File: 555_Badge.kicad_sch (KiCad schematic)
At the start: 13 parts

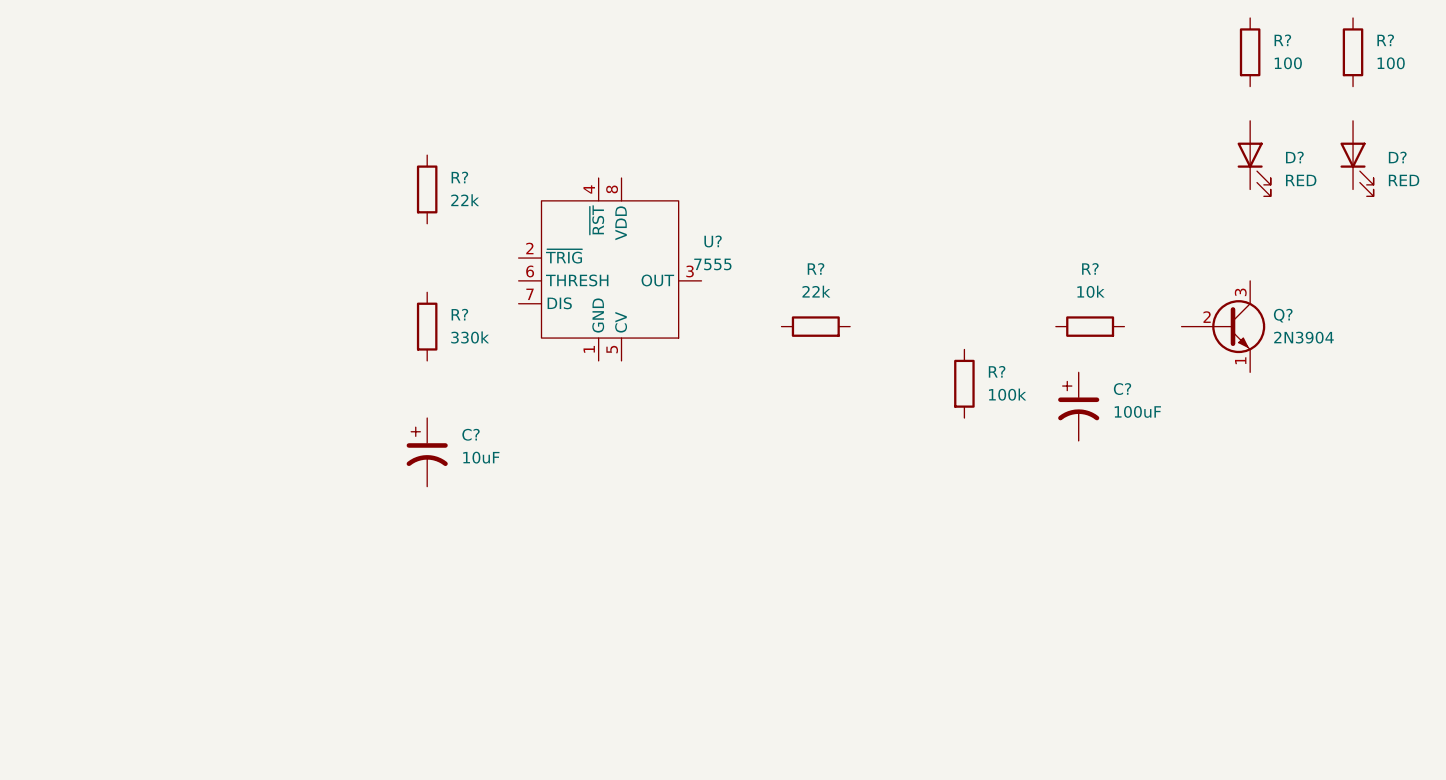
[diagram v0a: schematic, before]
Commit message: Small changes to the badge symbol and finished schematic
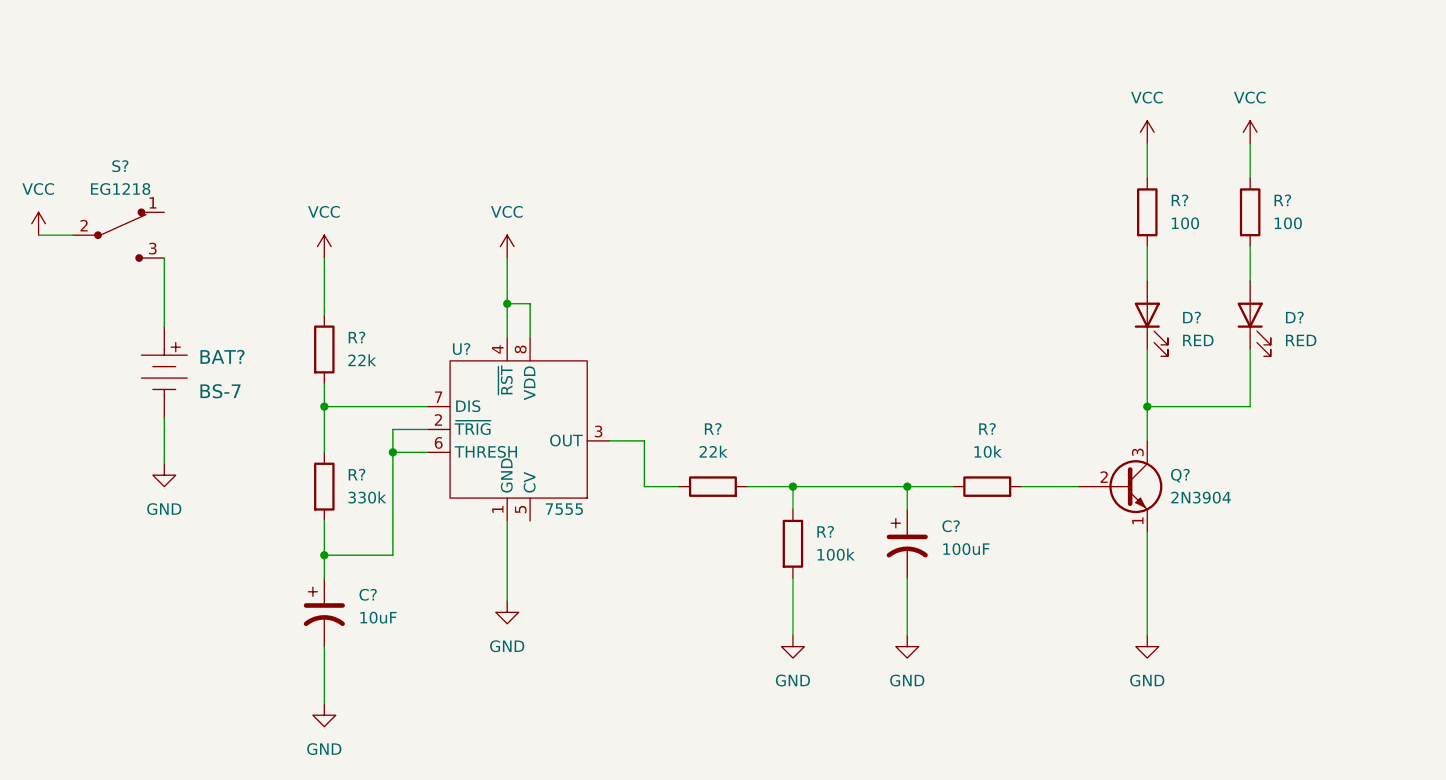
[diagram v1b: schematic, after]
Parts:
- added BAT?: BS-7, digikey-footprints:Battery_Holder_Coin_2032_BS-7, symbol dk_Battery-Holders-Clips-Contacts:BS-7
- added S?: EG1218, digikey-footprints:Switch_Slide_11.6x4mm_EG1218, symbol dk_Slide-Switches:EG1218
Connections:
- net at D?.1 (K): now also D?.1 (K), Q?.3 (C)
- net at D?.2 (A): now also R?.2 (x2)
- net at R?.1: now also C?.1, R?.1, R?.2
- net GND: now reaches R?.2
- net GND: now also C?.2, C?.2, Q?.1 (E), U?.1 (GND), BAT?.Neg
- net at R?.2: now also Q?.2 (B)
- net at U?.2 (~{TRIG}): now also C?.1, R?.2, U?.6 (THRESH)
- net at U?.3 (OUT): now also R?.1
- net VCC: now reaches U?.4 (~{RST})
- net VCC: now also R?.1, R?.1, R?.1, U?.8 (VDD), S?.2
- net at U?.7 (DIS): now also R?.1, R?.2
- new net: BAT?.Pos, S?.3
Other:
- moved on the sheet: C?, D?, Q?, R?, U?

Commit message: More changes to schematic. Numbered all of my resistors and capacitors
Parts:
- gave numbers to parts that had none: 15

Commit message: Lot of work on schematic and PCB to place components and begin constructing the PCB layout
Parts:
- C1: footprint (none) -> Capacitor_THT:CP_Radial_D5.0mm_P2.00mm
- C2: footprint (none) -> Capacitor_THT:CP_Radial_D6.3mm_P2.50mm
- D1, D2: footprint (none) -> LED_THT:LED_D3.0mm
- Q1: footprint Package_TO_SOT_THT:TO-92_Inline -> digikey-footprints:TO-92-3
- R1, R2, R3, R4, R5, R6, R7: footprint (none) -> Resistor_THT:R_Axial_DIN0207_L6.3mm_D2.5mm_P7.62mm_Horizontal
- U1: footprint (none) -> 555_Badge:ICM7555-PDIP
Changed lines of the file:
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@@
       (effects (font (size 1.27 1.27)) (justify right))
     )
-    (property "Footprint" "" (id 2) (at 207.01 86.36 0)
+    (property "Footprint" "LED_THT:LED_D3.0mm" (id 2) (at 207.01 86.36 0)
       (effects (font (size 1.27 1.27)) hide)
     )
@@
       (effects (font (size 1.27 1.27)) (justify left))
     )
-    (property "Footprint" "" (id 2) (at 154.432 111.76 90)
+    (property "Footprint" "Resistor_THT:R_Axial_DIN0207_L6.3mm_D2.5mm_P7.62mm_Horizontal" (id 2) (at 154.432 111.76 90)
       (effects (font (size 1.27 1.27)) hide)
     )
@@
     (property "Reference" "R5" (id 0) (at 177.8 99.06 90))
     (property "Value" "10k" (id 1) (at 177.8 101.6 90))
-    (property "Footprint" "" (id 2) (at 177.8 107.188 90)
+    (property "Footprint" "Resistor_THT:R_Axial_DIN0207_L6.3mm_D2.5mm_P7.62mm_Horizontal" (id 2) (at 177.8 107.188 90)
       (effects (font (size 1.27 1.27)) hide)
     )
@@
     (property "Reference" "U1" (id 0) (at 119.38 90.17 0))
     (property "Value" "7555" (id 1) (at 130.81 107.95 0))
-    (property "Footprint" "" (id 2) (at 125.73 100.33 0)
+    (property "Footprint" "555_Badge:ICM7555-PDIP" (id 2) (at 125.73 100.33 0)
       (effects (font (size 1.27 1.27)) hide)
     )
@@
       (effects (font (size 1.27 1.27)) (justify left))
     )
-    (property "Footprint" "" (id 2) (at 205.232 74.93 90)
+    (property "Footprint" "Resistor_THT:R_Axial_DIN0207_L6.3mm_D2.5mm_P7.62mm_Horizontal" (id 2) (at 205.232 74.93 90)
       (effects (font (size 1.27 1.27)) hide)
     )
@@
       (effects (font (size 1.27 1.27)) (justify left))
     )
-    (property "Footprint" "" (id 2) (at 102.362 105.41 90)
+    (property "Footprint" "Resistor_THT:R_Axial_DIN0207_L6.3mm_D2.5mm_P7.62mm_Horizontal" (id 2) (at 102.362 105.41 90)
       (effects (font (size 1.27 1.27)) hide)
     )
@@
     (property "Reference" "R3" (id 0) (at 147.32 99.06 90))
     (property "Value" "22k" (id 1) (at 147.32 101.6 90))
-    (property "Footprint" "" (id 2) (at 147.32 107.188 90)
+    (property "Footprint" "Resistor_THT:R_Axial_DIN0207_L6.3mm_D2.5mm_P7.62mm_Horizontal" (id 2) (at 147.32 107.188 90)
       (effects (font (size 1.27 1.27)) hide)
     )
@@
       (effects (font (size 1.27 1.27)) (justify right))
     )
-    (property "Footprint" "" (id 2) (at 195.58 86.36 0)
+    (property "Footprint" "LED_THT:LED_D3.0mm" (id 2) (at 195.58 86.36 0)
       (effects (font (size 1.27 1.27)) hide)
     )
@@
       (effects (font (size 1.27 1.27)) (justify left))
     )
-    (property "Footprint" "" (id 2) (at 102.362 90.17 90)
+    (property "Footprint" "Resistor_THT:R_Axial_DIN0207_L6.3mm_D2.5mm_P7.62mm_Horizontal" (id 2) (at 102.362 90.17 90)
       (effects (font (size 1.27 1.27)) hide)
     )
@@
       (effects (font (size 1.27 1.27)) (justify left))
     )
-    (property "Footprint" "" (id 2) (at 168.91 111.76 0)
+    (property "Footprint" "Capacitor_THT:CP_Radial_D6.3mm_P2.50mm" (id 2) (at 168.91 111.76 0)
       (effects (font (size 1.27 1.27)) hide)
     )
@@
       (effects (font (size 1.27 1.27)) (justify left))
     )
-    (property "Footprint" "" (id 2) (at 193.802 74.93 90)
+    (property "Footprint" "Resistor_THT:R_Axial_DIN0207_L6.3mm_D2.5mm_P7.62mm_Horizontal" (id 2) (at 193.802 74.93 90)
       (effects (font (size 1.27 1.27)) hide)
     )
@@
       (effects (font (size 1.27 1.27)) (justify left))
     )
-    (property "Footprint" "Package_TO_SOT_THT:TO-92_Inline" (id 2) (at 198.12 107.315 0)
+    (property "Footprint" "digikey-footprints:TO-92-3" (id 2) (at 198.12 107.315 0)
       (effects (font (size 1.27 1.27) italic) (justify left) hide)
     )
@@
       (effects (font (size 1.27 1.27)) (justify left))
     )
-    (property "Footprint" "" (id 2) (at 104.14 119.38 0)
+    (property "Footprint" "Capacitor_THT:CP_Radial_D5.0mm_P2.00mm" (id 2) (at 104.14 119.38 0)
       (effects (font (size 1.27 1.27)) hide)
     )
@@
     )
     (path "/d3fa06eb-1b81-4ee1-a0d5-48e6562647a9"
-      (reference "C1") (unit 1) (value "10uF") (footprint "")
+      (reference "C1") (unit 1) (value "10uF") (footprint "Capacitor_THT:CP_Radial_D5.0mm_P2.00mm")
     )
     (path "/ac885c2b-acf9-4710-8331-7fa61f783572"
-      (reference "C2") (unit 1) (value "100uF") (footprint "")
+      (reference "C2") (unit 1) (value "100uF") (footprint "Capacitor_THT:CP_Radial_D6.3mm_P2.50mm")
     )
     (path "/71e89c5f-6755-44c0-b2b9-01f2a78a5086"
-      (reference "D1") (unit 1) (value "RED") (footprint "")
+      (reference "D1") (unit 1) (value "RED") (footprint "LED_THT:LED_D3.0mm")
     )
     (path "/0494f7e3-4dd9-4121-a1cc-1815d0db5c07"
-      (reference "D2") (unit 1) (value "RED") (footprint "")
+      (reference "D2") (unit 1) (value "RED") (footprint "LED_THT:LED_D3.0mm")
     )
     (path "/cef4e043-6413-4f3d-acfa-55bc594a5e3c"
-      (reference "Q1") (unit 1) (value "2N3904") (footprint "Package_TO_SOT_THT:TO-92_Inline")
+      (reference "Q1") (unit 1) (value "2N3904") (footprint "digikey-footprints:TO-92-3")
     )
     (path "/93cbdd14-26c5-4d16-91fc-887a6c5e22fd"
-      (reference "R1") (unit 1) (value "22k") (footprint "")
+      (reference "R1") (unit 1) (value "22k") (footprint "Resistor_THT:R_Axial_DIN0207_L6.3mm_D2.5mm_P7.62mm_Horizontal")
     )
     (path "/5297de71-a6b5-4891-9d2a-d01dde0db7fe"
-      (reference "R2") (unit 1) (value "330k") (footprint "")
+      (reference "R2") (unit 1) (value "330k") (footprint "Resistor_THT:R_Axial_DIN0207_L6.3mm_D2.5mm_P7.62mm_Horizontal")
     )
     (path "/5d66ca21-1dcb-496f-ab75-846e2dca23a6"
-      (reference "R3") (unit 1) (value "22k") (footprint "")
+      (reference "R3") (unit 1) (value "22k") (footprint "Resistor_THT:R_Axial_DIN0207_L6.3mm_D2.5mm_P7.62mm_Horizontal")
     )
     (path "/188260ef-b4db-4c72-abe5-7930b4c5a7a0"
-      (reference "R4") (unit 1) (value "100k") (footprint "")
+      (reference "R4") (unit 1) (value "100k") (footprint "Resistor_THT:R_Axial_DIN0207_L6.3mm_D2.5mm_P7.62mm_Horizontal")
     )
     (path "/34a09159-9083-4dcc-b816-2f400f77b90d"
-      (reference "R5") (unit 1) (value "10k") (footprint "")
+      (reference "R5") (unit 1) (value "10k") (footprint "Resistor_THT:R_Axial_DIN0207_L6.3mm_D2.5mm_P7.62mm_Horizontal")
     )
     (path "/be0edc49-faef-4d32-8ee2-f57671e41c85"
-      (reference "R6") (unit 1) (value "100") (footprint "")
+      (reference "R6") (unit 1) (value "100") (footprint "Resistor_THT:R_Axial_DIN0207_L6.3mm_D2.5mm_P7.62mm_Horizontal")
     )
     (path "/4baaa53c-63b6-4fcd-902b-44e3a368db82"
-      (reference "R7") (unit 1) (value "100") (footprint "")
+      (reference "R7") (unit 1) (value "100") (footprint "Resistor_THT:R_Axial_DIN0207_L6.3mm_D2.5mm_P7.62mm_Horizontal")
     )
     (path "/aeea1a68-1ae4-450b-be91-e44f63e84970"
@@
     )
     (path "/37882845-ff70-43bc-9510-b0d6b650754c"
-      (reference "U1") (unit 1) (value "7555") (footprint "")
-    )
-  )
+      (reference "U1") (unit 1) (value "7555") (footprint "555_Badge:ICM7555-PDIP")
+    )
+  )
